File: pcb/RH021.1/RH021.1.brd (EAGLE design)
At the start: 36 x 32 mm, 39 parts, among them U1 ATTINY84, U2 OPA344, U3 ADMP401

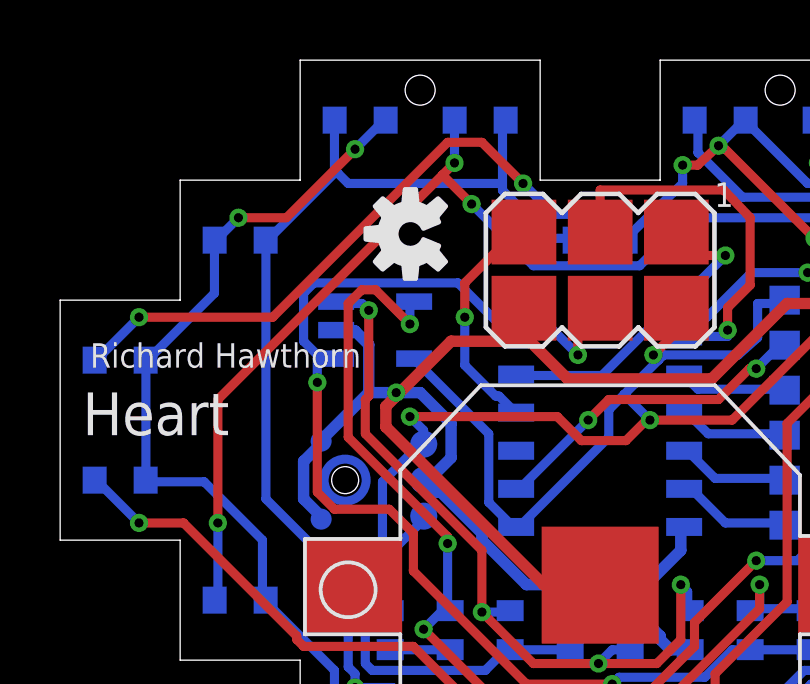
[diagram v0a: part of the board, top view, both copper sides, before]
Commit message: swap 2 leds
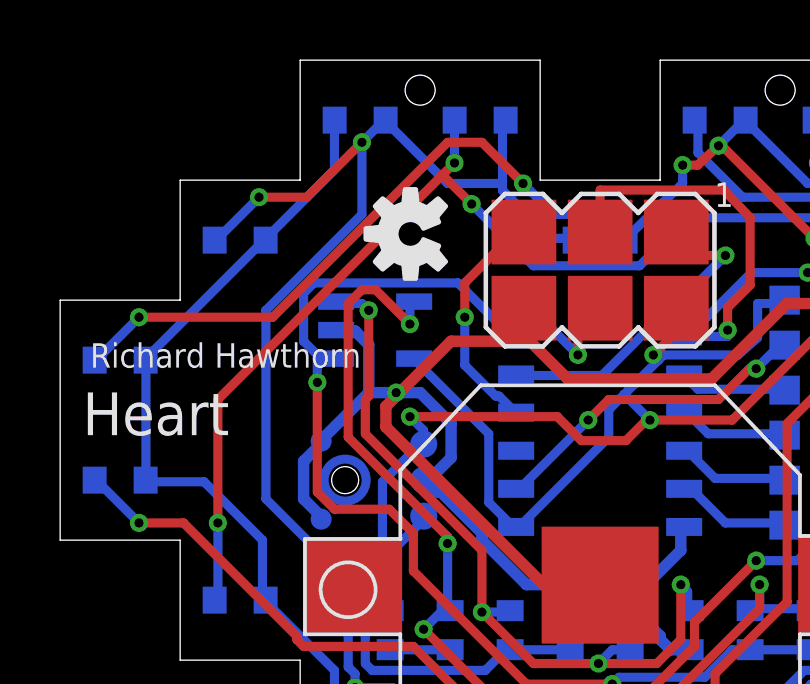
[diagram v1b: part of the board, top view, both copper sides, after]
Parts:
- moved LED16 5.66 mm to (6.00, 26.0)
- moved LED17 5.66 mm to (10.0, 30.0)
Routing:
- net N$22: track 66.0 -> 72.0 mm, vias 4 -> 6
- net N$12: track 89.0 -> 87.4 mm, vias 2 -> 0
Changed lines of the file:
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@@
 <setting verticaltext="up"/>
 </settings>
-<grid distance="0.25" unitdist="mm" unit="mm" style="lines" multiple="1" display="yes" altdistance="0.1" altunitdist="mm" altunit="mm"/>
+<grid distance="2" unitdist="mm" unit="mm" style="lines" multiple="1" display="yes" altdistance="0.1" altunitdist="mm" altunit="mm"/>
 <layers>
 <layer number="1" name="Top" color="4" fill="1" visible="yes" active="yes"/>
@@
 <element name="LED8" library="LowPowerLab" package="0603-LED" value="LED0603" x="26" y="10" smashed="yes" rot="MR0"/>
 <element name="LED3" library="LowPowerLab" package="0603-LED" value="LED0603" x="26" y="30" smashed="yes" rot="MR0"/>
-<element name="LED17" library="LowPowerLab" package="0603-LED" value="LED0603" x="6" y="26" smashed="yes" rot="MR0"/>
+<element name="LED17" library="LowPowerLab" package="0603-LED" value="LED0603" x="10" y="30" smashed="yes" rot="MR0"/>
 <element name="LED12" library="LowPowerLab" package="0603-LED" value="LED0603" x="10" y="10" smashed="yes" rot="MR0"/>
 <element name="LED7" library="LowPowerLab" package="0603-LED" value="LED0603" x="30" y="14" smashed="yes" rot="MR0"/>
 <element name="LED2" library="LowPowerLab" package="0603-LED" value="LED0603" x="22" y="30" smashed="yes" rot="MR0"/>
-<element name="LED16" library="LowPowerLab" package="0603-LED" value="LED0603" x="10" y="30" smashed="yes" rot="MR0"/>
+<element name="LED16" library="LowPowerLab" package="0603-LED" value="LED0603" x="6" y="26" smashed="yes" rot="MR0"/>
 <element name="LED11" library="LowPowerLab" package="0603-LED" value="LED0603" x="14" y="6" smashed="yes" rot="MR0"/>
 <element name="LED6" library="LowPowerLab" package="0603-LED" value="LED0603" x="34" y="18" smashed="yes" rot="MR0"/>
@@
 <wire x1="2.8575" y1="18.0594" x2="2.85" y2="18" width="0.3048" layer="16"/>
 <wire x1="2.8575" y1="21.9456" x2="2.85" y2="22" width="0.3048" layer="16"/>
-<wire x1="5.1435" y1="24.2316" x2="5.1435" y2="25.9461" width="0.3048" layer="16"/>
-<wire x1="2.9718" y1="22.0599" x2="5.1435" y2="24.2316" width="0.3048" layer="16"/>
-<wire x1="5.1435" y1="25.9461" x2="5.15" y2="26" width="0.3048" layer="16"/>
 <wire x1="2.9718" y1="22.0599" x2="2.85" y2="22" width="0.3048" layer="16"/>
-<wire x1="9.8298" y1="29.0322" x2="10.7442" y2="29.9466" width="0.3048" layer="16"/>
-<wire x1="7.5438" y1="26.7462" x2="9.8298" y2="29.0322" width="0.3048" layer="1"/>
-<wire x1="5.9436" y1="26.7462" x2="7.5438" y2="26.7462" width="0.3048" layer="1"/>
-<wire x1="5.2578" y1="26.0604" x2="5.9436" y2="26.7462" width="0.3048" layer="16"/>
-<wire x1="10.7442" y1="29.9466" x2="10.85" y2="30" width="0.3048" layer="16"/>
-<wire x1="5.2578" y1="26.0604" x2="5.15" y2="26" width="0.3048" layer="16"/>
 <wire x1="6.7437" y1="16.002" x2="6.7437" y2="14.0589" width="0.3048" layer="16"/>
 <wire x1="4.8006" y1="17.9451" x2="6.7437" y2="16.002" width="0.3048" layer="16"/>
@@
 <wire x1="9.2583" y1="9.9441" x2="9.15" y2="10" width="0.3048" layer="16"/>
 <wire x1="29.0322" y1="13.9446" x2="29.15" y2="14" width="0.3048" layer="16"/>
-<via x="9.8298" y="29.0322" extent="1-16" drill="0.3048"/>
-<via x="5.9436" y="26.7462" extent="1-16" drill="0.3048"/>
+<wire x1="9.144" y1="28.3464" x2="6.858" y2="26.0604" width="0.3048" layer="16"/>
+<wire x1="9.144" y1="29.9466" x2="9.144" y2="28.3464" width="0.3048" layer="16"/>
+<wire x1="6.858" y1="26.0604" x2="6.85" y2="26" width="0.3048" layer="16"/>
+<wire x1="9.144" y1="29.9466" x2="9.15" y2="30" width="0.3048" layer="16"/>
+<wire x1="2.9718" y1="22.1742" x2="6.7437" y2="25.9461" width="0.3048" layer="16"/>
+<wire x1="6.7437" y1="25.9461" x2="6.85" y2="26" width="0.3048" layer="16"/>
+<wire x1="2.9718" y1="22.1742" x2="2.85" y2="22" width="0.3048" layer="16"/>
 </signal>
 <signal name="N$22">
@@
 <wire x1="33.147" y1="17.9451" x2="33.15" y2="18" width="0.3048" layer="16"/>
 <wire x1="25.9461" y1="16.5735" x2="25.85" y2="16.5" width="0.3048" layer="16"/>
-<wire x1="16.3449" y1="26.0604" x2="17.145" y2="26.0604" width="0.3048" layer="16"/>
-<wire x1="14.7447" y1="27.6606" x2="16.3449" y2="26.0604" width="0.3048" layer="16"/>
-<wire x1="14.7447" y1="29.9466" x2="14.7447" y2="27.8892" width="0.3048" layer="16"/>
-<wire x1="14.7447" y1="27.8892" x2="14.7447" y2="27.6606" width="0.3048" layer="16"/>
-<wire x1="17.145" y1="26.0604" x2="17.15" y2="26" width="0.3048" layer="16"/>
-<wire x1="14.7447" y1="29.9466" x2="14.85" y2="30" width="0.3048" layer="16"/>
 <wire x1="13.1445" y1="7.7724" x2="13.1445" y2="6.0579" width="0.3048" layer="16"/>
 <wire x1="9.8298" y1="11.0871" x2="13.1445" y2="7.7724" width="0.3048" layer="1"/>
@@
 <wire x1="9.6012" y1="14.6304" x2="9.6012" y2="11.7729" width="0.3048" layer="16"/>
 <wire x1="6.858" y1="17.3736" x2="9.6012" y2="14.6304" width="0.3048" layer="16"/>
-<wire x1="6.858" y1="25.9461" x2="6.858" y2="17.3736" width="0.3048" layer="16"/>
 <wire x1="13.1445" y1="6.0579" x2="13.15" y2="6" width="0.3048" layer="16"/>
-<wire x1="6.858" y1="25.9461" x2="6.85" y2="26" width="0.3048" layer="16"/>
-<wire x1="9.144" y1="28.2321" x2="9.144" y2="29.9466" width="0.3048" layer="16"/>
-<wire x1="6.9723" y1="26.0604" x2="9.144" y2="28.2321" width="0.3048" layer="16"/>
-<wire x1="9.144" y1="29.9466" x2="9.15" y2="30" width="0.3048" layer="16"/>
-<wire x1="6.9723" y1="26.0604" x2="6.85" y2="26" width="0.3048" layer="16"/>
-<wire x1="9.6012" y1="27.8892" x2="14.7447" y2="27.8892" width="0.3048" layer="16"/>
-<wire x1="9.2583" y1="28.2321" x2="9.6012" y2="27.8892" width="0.3048" layer="16"/>
-<wire x1="9.2583" y1="28.2321" x2="9.144" y2="28.2321" width="0.3048" layer="16"/>
 <wire x1="24.5745" y1="15.3162" x2="25.7175" y2="16.4592" width="0.3048" layer="16"/>
 <wire x1="23.2029" y1="15.3162" x2="24.5745" y2="15.3162" width="0.3048" layer="16"/>
@@
 <via x="23.2029" y="15.3162" extent="1-16" drill="0.3048"/>
 <via x="19.2024" y="10.5156" extent="1-16" drill="0.3048"/>
+<wire x1="14.7447" y1="27.6606" x2="14.7447" y2="27.8892" width="0.3048" layer="16"/>
+<wire x1="14.7447" y1="27.8892" x2="14.7447" y2="29.9466" width="0.3048" layer="16"/>
+<wire x1="16.3449" y1="26.0604" x2="14.7447" y2="27.6606" width="0.3048" layer="16"/>
+<wire x1="17.145" y1="26.0604" x2="16.3449" y2="26.0604" width="0.3048" layer="16"/>
+<wire x1="14.7447" y1="29.9466" x2="14.85" y2="30" width="0.3048" layer="16"/>
+<wire x1="17.145" y1="26.0604" x2="17.15" y2="26" width="0.3048" layer="16"/>
+<wire x1="6.6294" y1="27.432" x2="5.2578" y2="26.0604" width="0.3048" layer="16"/>
+<wire x1="8.2296" y1="27.432" x2="6.6294" y2="27.432" width="0.3048" layer="1"/>
+<wire x1="10.0584" y1="29.2608" x2="8.2296" y2="27.432" width="0.3048" layer="1"/>
+<wire x1="10.7442" y1="29.9466" x2="10.0584" y2="29.2608" width="0.3048" layer="16"/>
+<wire x1="5.2578" y1="26.0604" x2="5.15" y2="26" width="0.3048" layer="16"/>
+<wire x1="10.7442" y1="29.9466" x2="10.85" y2="30" width="0.3048" layer="16"/>
+<wire x1="12.9159" y1="27.8892" x2="14.7447" y2="27.8892" width="0.3048" layer="16"/>
+<wire x1="10.8585" y1="29.9466" x2="12.9159" y2="27.8892" width="0.3048" layer="16"/>
+<wire x1="10.8585" y1="29.9466" x2="10.85" y2="30" width="0.3048" layer="16"/>
+<wire x1="10.0584" y1="26.8605" x2="10.0584" y2="29.2608" width="0.3048" layer="16"/>
+<wire x1="6.858" y1="23.6601" x2="10.0584" y2="26.8605" width="0.3048" layer="16"/>
+<wire x1="6.858" y1="17.3736" x2="6.858" y2="23.6601" width="0.3048" layer="16"/>
+<via x="6.6294" y="27.432" extent="1-16" drill="0.3048"/>
+<via x="10.0584" y="29.2608" extent="1-16" drill="0.3048"/>
 </signal>
 <signal name="C7N$1">
